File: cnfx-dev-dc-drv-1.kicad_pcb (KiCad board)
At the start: 2 copper layers, 51.3 x 51.3 mm, 66 parts, among them J1 Conn_01x03, J2 TC2030, J3 Conn_01x02, J4 Conn_01x02, J5 Conn_01x04_Pin, J6 Conn_01x02, J7 Conn_01x02, SW1 SW_Push, SW2 SW_Push, SW3 SW_Push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

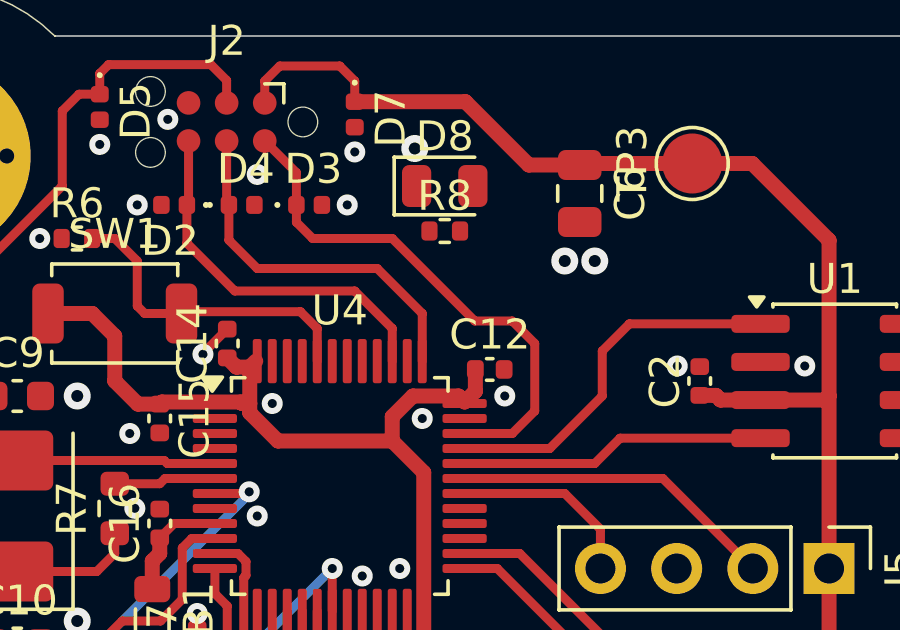
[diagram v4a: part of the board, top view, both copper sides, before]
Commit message: pcb: add can status led routing
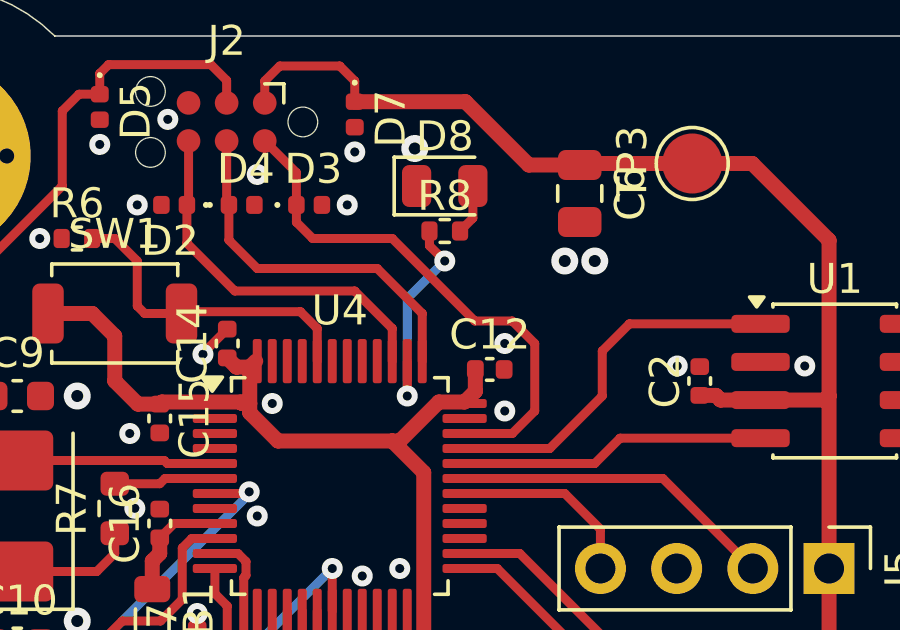
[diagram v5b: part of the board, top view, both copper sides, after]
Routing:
- net Net-(U4-PA15): track 0.00 -> 7.39 mm, vias 0 -> 2
- net Net-(D8-A): track 0.00 -> 1.68 mm
- net +3V3: track 164.4 -> 163.8 mm
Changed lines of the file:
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@@
 	)
 	(via
-		(at 119 68)
+		(at 119 68.5)
 		(size 0.7)
 		(drill 0.3)
@@
 	)
 	(via
-		(at 116.25 68.75)
-		(size 0.7)
-		(drill 0.3)
-		(layers "F.Cu" "B.Cu")
-		(free yes)
-		(net "GND")
-	)
-	(via
 		(at 123.965 92.25)
 		(size 0.9)
@@
 		(size 0.9)
 		(drill 0.4)
+		(layers "F.Cu" "B.Cu")
+		(free yes)
+		(net "GND")
+	)
+	(via
+		(at 119 66.25)
+		(size 0.7)
+		(drill 0.3)
 		(layers "F.Cu" "B.Cu")
 		(free yes)
@@
 	)
 	(segment
-		(start 115.939339 68)
-		(end 117.4625 68)
-		(width 0.5)
-		(layer "F.Cu")
-		(net "+3V3")
-	)
-	(segment
 		(start 110.24883 68.25)
 		(end 110.5 68.25)
@@
 		(start 119.8 60.3)
 		(end 117.69 58.19)
-		(width 0.5)
-		(layer "F.Cu")
-		(net "+3V3")
-	)
-	(segment
-		(start 115.25 68.689339)
-		(end 115.939339 68)
 		(width 0.5)
 		(layer "F.Cu")
@@
 	)
 	(segment
+		(start 115.50117 69.5)
+		(end 116.80117 68.2)
+		(width 0.5)
+		(layer "F.Cu")
+		(net "+3V3")
+	)
+	(segment
 		(start 127.25 60.25)
 		(end 125.25 60.25)
@@
 	)
 	(segment
-		(start 117.4625 68)
-		(end 117.6625 68.2)
-		(width 0.5)
-		(layer "F.Cu")
-		(net "+3V3")
-	)
-	(segment
 		(start 116.75 92.25)
 		(end 116.75 92.8)
@@
 	)
 	(segment
+		(start 118.02 67.8425)
+		(end 118.02 67.115)
+		(width 0.5)
+		(layer "F.Cu")
+		(net "+3V3")
+	)
+	(segment
 		(start 126.038216 67.98)
 		(end 126.193216 68.135)
@@
 	)
 	(segment
-		(start 118.02 67.115)
-		(end 118.02 67.8425)
-		(width 0.5)
-		(layer "F.Cu")
-		(net "+3V3")
-	)
-	(segment
-		(start 118.02 67.8425)
+		(start 116.80117 68.2)
 		(end 117.6625 68.2)
 		(width 0.5)
@@
 	)
 	(segment
-		(start 115.25 69.5)
-		(end 115.25 68.689339)
-		(width 0.5)
-		(layer "F.Cu")
-		(net "+3V3")
-	)
-	(segment
 		(start 129.81 73.75)
 		(end 129.81 85.06)
+		(width 0.5)
+		(layer "F.Cu")
+		(net "+3V3")
+	)
+	(segment
+		(start 115.25 69.5)
+		(end 115.50117 69.5)
+		(width 0.5)
+		(layer "F.Cu")
+		(net "+3V3")
+	)
+	(segment
+		(start 117.6625 68.2)
+		(end 118.02 67.8425)
 		(width 0.5)
 		(layer "F.Cu")
@@
 	)
 	(segment
+		(start 117.51 62.5)
+		(end 117.9375 62.0725)
+		(width 0.3)
+		(layer "F.Cu")
+		(net "Net-(D8-A)")
+	)
+	(segment
+		(start 117.9375 62.0725)
+		(end 117.9375 61)
+		(width 0.3)
+		(layer "F.Cu")
+		(net "Net-(D8-A)")
+	)
+	(segment
 		(start 140.6 69.52)
 		(end 140.6 77.14)
@@
 	)
 	(segment
+		(start 116.49 62.5)
+		(end 116.49 62.99)
+		(width 0.3)
+		(layer "F.Cu")
+		(net "Net-(U4-PA15)")
+	)
+	(segment
+		(start 116.49 62.99)
+		(end 117 63.5)
+		(width 0.3)
+		(layer "F.Cu")
+		(net "Net-(U4-PA15)")
+	)
+	(segment
+		(start 115.75 66.8375)
+		(end 115.75 68)
+		(width 0.3)
+		(layer "F.Cu")
+		(net "Net-(U4-PA15)")
+	)
+	(via
+		(at 117 63.5)
+		(size 0.7)
+		(drill 0.3)
+		(layers "F.Cu" "B.Cu")
+		(net "Net-(U4-PA15)")
+	)
+	(via
+		(at 115.75 68)
+		(size 0.7)
+		(drill 0.3)
+		(layers "F.Cu" "B.Cu")
+		(net "Net-(U4-PA15)")
+	)
+	(segment
+		(start 115.75 64.75)
+		(end 117 63.5)
+		(width 0.3)
+		(layer "B.Cu")
+		(net "Net-(U4-PA15)")
+	)
+	(segment
+		(start 115.75 68)
+		(end 115.75 64.75)
+		(width 0.3)
+		(layer "B.Cu")
+		(net "Net-(U4-PA15)")
+	)
+	(segment

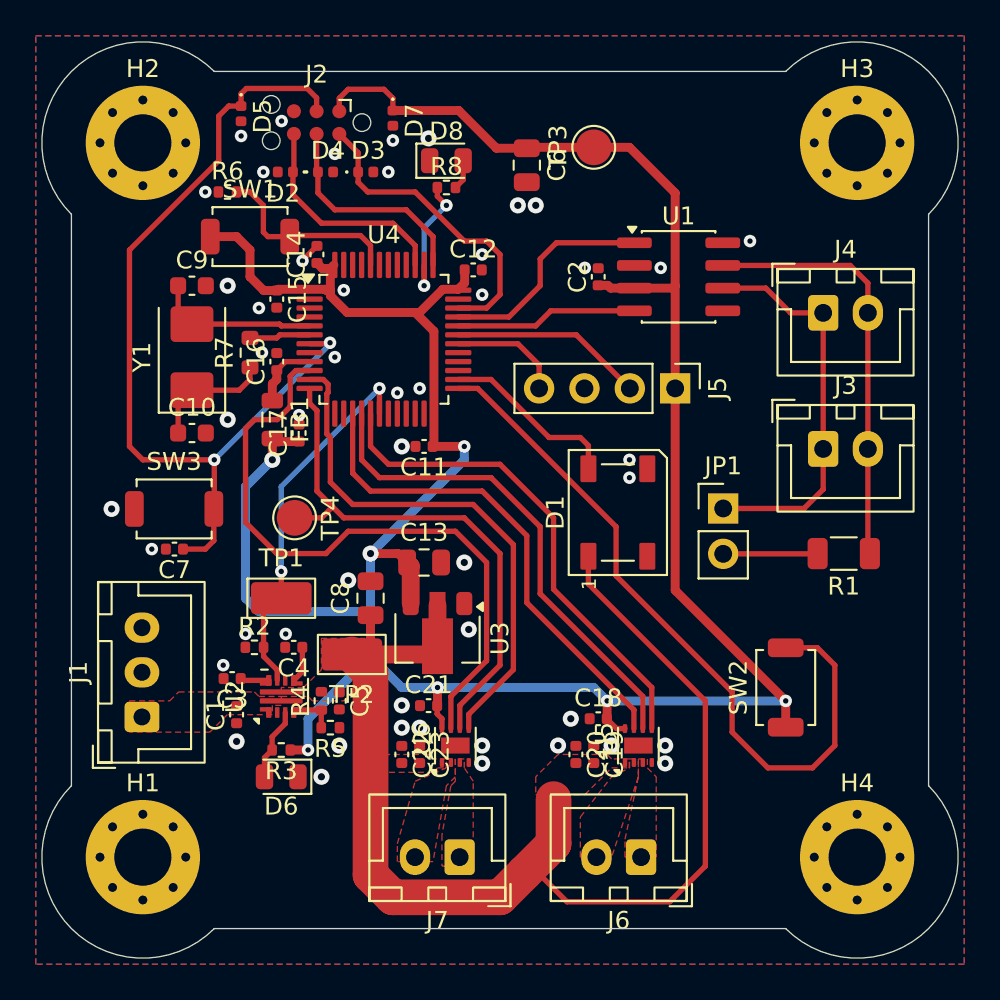
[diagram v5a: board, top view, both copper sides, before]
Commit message: pcb: add stitching vias
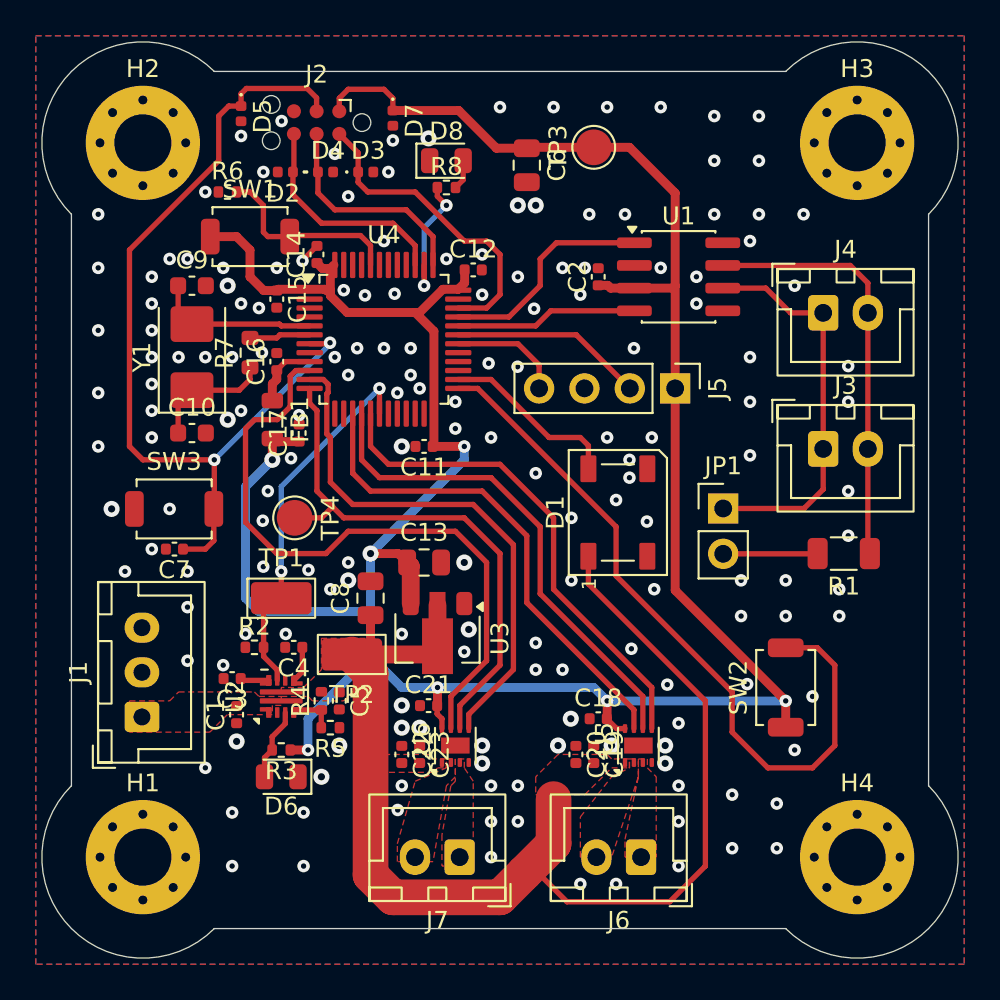
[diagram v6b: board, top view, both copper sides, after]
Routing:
- net GND: vias 49 -> 171
